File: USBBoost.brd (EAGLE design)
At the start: 43.8 x 20.3 mm, 27 parts, among them IC1 RT9276, J1 Input, J2 3.75V, J3 2.33V, J4 1.17V, J5 Status, X1 USB_

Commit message: foo
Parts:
- removed R15: 20k0, freetronics-original:0603
- added R3: 49k9, freetronics-original:0603
- R10: value 1k -> 130k
- R11: value 130k -> 73k2
- R12: value 73k2 -> 26k7
- R13: value 26k7 -> 20k
- R14: value 20k -> 20k0
- R5: value 49k9 -> 180k
- R6: value 180k -> 10k
- R8: value 10k -> 1k
- moved R8 17.0 mm to (15.9, 17.8), turned to 90 degrees
- moved R7 15.8 mm to (27.1, 5.08), turned to 0 degrees
- moved R14 9.38 mm to (18.4, 8.49), turned to 180 degrees
- moved R5 8.10 mm to (18.4, 6.83), turned to 180 degrees
- moved R6 7.21 mm to (12.4, 10.8), turned to 270 degrees
- moved R13 6.98 mm to (10.8, 14.0), turned to 270 degrees
- moved R10 6.35 mm to (8.89, 14.0)
- moved R12 2.86 mm to (3.81, 14.0)
- moved R4 2.77 mm to (26.0, 9.53), turned to 270 degrees
- moved R11 2.22 mm to (6.67, 14.0), turned to 180 degrees
- moved R9 1.90 mm to (14.0, 17.8)
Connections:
- net !LBO: now also R7.2; no longer R8.2
- net !PGOOD: now also R6.2; no longer R7.2
- net FB: now also R14.2, R5.2; no longer R15.2, R6.2
- net GND: now also R13.1, R3.2; no longer R15.1, R5.2
- net LBI: now also R10.1, R13.2; no longer R13.1, R14.2
- net N$10: now also R4.1; no longer R5.1
- net N$11: now also R11.2; no longer R12.2
- net N$12: now also R12.2; no longer R13.2
- net N$15: now also R9.2; no longer R10.2
- net N$5: now also R10.2; no longer R11.2
- net N$7: now also R3.1; no longer R4.1
- net N$8: now also R8.2; no longer R9.2
- net VOUT: now also R5.1; no longer R10.1
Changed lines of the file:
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@@
 <elements>
 <element name="C1" library="freetronics-jon" package="C0805" value="10uF" x="6.35" y="11.1125" smashed="yes"/>
-<element name="R15" library="freetronics-original" package="0603" value="20k0" x="18.415" y="8.493125" smashed="yes" rot="R180"/>
-<element name="R6" library="freetronics-original" package="0603" value="180k" x="18.399225" y="6.82625" smashed="yes" rot="R180"/>
+<element name="R14" library="freetronics-original" package="0603" value="20k0" x="18.415" y="8.493125" smashed="yes" rot="R180"/>
+<element name="R5" library="freetronics-original" package="0603" value="180k" x="18.399225" y="6.82625" smashed="yes" rot="R180"/>
 <element name="C2" library="freetronics-jon" package="C1206K" value="22uF" x="18.0975" y="3.4924" smashed="yes" rot="R90"/>
-<element name="R9" library="freetronics-original" package="0603" value="1k" x="15.875" y="17.78" smashed="yes" rot="R90"/>
+<element name="R8" library="freetronics-original" package="0603" value="1k" x="15.875" y="17.78" smashed="yes" rot="R90"/>
 <element name="J1" library="freetronics-master-v1" package="1X02" value="Input" x="1.90495" y="11.43" smashed="yes" rot="R270"/>
 <element name="X1" library="freetronics-master-v1" package="USB-A-S-SILK-FEMALE" value="USB_" x="36.83" y="10.16" smashed="yes" rot="R180"/>
 <element name="R2" library="freetronics-original" package="0603" value="75k" x="26.035" y="12.7" smashed="yes" rot="R270"/>
-<element name="R5" library="freetronics-original" package="0603" value="49k9" x="26.035" y="9.525" smashed="yes" rot="R270"/>
+<element name="R4" library="freetronics-original" package="0603" value="49k9" x="26.035" y="9.525" smashed="yes" rot="R270"/>
 <element name="R1" library="freetronics-original" package="0603" value="75k" x="22.621875" y="11.27125" smashed="yes" rot="R270"/>
-<element name="R4" library="freetronics-original" package="0603" value="49k9" x="23.33625" y="8.89" smashed="yes"/>
+<element name="R3" library="freetronics-original" package="0603" value="49k9" x="23.33625" y="8.89" smashed="yes"/>
 <element name="LED1" library="freetronics-master-v1" package="LED-0603" value="Power" x="17.78" y="17.78" smashed="yes" rot="R270"/>
 <element name="L1" library="freetronics-luke" package="CDRH" value="6.8 uH" x="7.62" y="5.715" smashed="yes" rot="R180"/>
@@
 <element name="J3" library="freetronics-luke" package="SJ" value="2.33V" x="6.35" y="17.145" smashed="yes" rot="R90"/>
 <element name="J4" library="freetronics-luke" package="SJ" value="1.17V" x="3.81" y="17.145" smashed="yes" rot="R90"/>
-<element name="R13" library="freetronics-original" package="0603" value="26k7" x="3.81" y="13.97" smashed="yes" rot="R180"/>
-<element name="R12" library="freetronics-original" package="0603" value="73k2" x="6.6675" y="13.97" smashed="yes" rot="R180"/>
-<element name="R11" library="freetronics-original" package="0603" value="130k" x="8.89" y="13.97" smashed="yes" rot="R90"/>
-<element name="R14" library="freetronics-original" package="0603" value="20k" x="10.795" y="13.97" smashed="yes" rot="R270"/>
-<element name="R7" library="freetronics-original" package="0603" value="10k" x="12.3825" y="10.795" smashed="yes" rot="R270"/>
-<element name="R8" library="freetronics-original" package="0603" value="10k" x="27.14625" y="5.08" smashed="yes"/>
-<element name="R10" library="freetronics-original" package="0603" value="1k" x="13.97" y="17.78" smashed="yes" rot="R90"/>
+<element name="R12" library="freetronics-original" package="0603" value="26k7" x="3.81" y="13.97" smashed="yes" rot="R180"/>
+<element name="R11" library="freetronics-original" package="0603" value="73k2" x="6.6675" y="13.97" smashed="yes" rot="R180"/>
+<element name="R10" library="freetronics-original" package="0603" value="130k" x="8.89" y="13.97" smashed="yes" rot="R90"/>
+<element name="R13" library="freetronics-original" package="0603" value="20k" x="10.795" y="13.97" smashed="yes" rot="R270"/>
+<element name="R6" library="freetronics-original" package="0603" value="10k" x="12.3825" y="10.795" smashed="yes" rot="R270"/>
+<element name="R7" library="freetronics-original" package="0603" value="10k" x="27.14625" y="5.08" smashed="yes"/>
+<element name="R9" library="freetronics-original" package="0603" value="1k" x="13.97" y="17.78" smashed="yes" rot="R90"/>
 <element name="LED2" library="freetronics-master-v1" package="LED-0603" value="Low Batt" x="12.065" y="17.78" smashed="yes" rot="R270"/>
 <element name="J5" library="freetronics-master-v1" package="1X02" value="Status" x="28.575" y="2.54" smashed="yes" rot="R180"/>
@@
 <signal name="GND">
 <contactref element="C1" pad="2"/>
-<contactref element="R15" pad="1"/>
+<contactref element="R14" pad="1"/>
 <contactref element="C2" pad="2"/>
-<contactref element="R5" pad="2"/>
 <contactref element="R4" pad="2"/>
+<contactref element="R3" pad="2"/>
 <contactref element="LED1" pad="C"/>
 <polygon width="0.4064" layer="1" isolate="0.4064">
@@
 <vertex x="-0.635" y="0"/>
 </polygon>
-<contactref element="R14" pad="1"/>
+<contactref element="R13" pad="1"/>
 <contactref element="J1" pad="2"/>
 <contactref element="X1" pad="GND"/>
@@
 <via x="10.795" y="15.875" extent="1-16" drill="0.5"/>
 <via x="15.875" y="14.605" extent="1-16" drill="0.5"/>
-<wire x1="14.97" y1="4.24" x2="15.67" y2="4.24" width="0.3048" layer="1"/>
+<wire x1="14.97" y1="4.24" x2="15.67" y2="4.24" width="0.2794" layer="1"/>
 <wire x1="15.67" y1="4.24" x2="15.875" y2="4.445" width="0.3048" layer="1"/>
 <wire x1="15.875" y1="4.445" x2="15.875" y2="5.23875" width="0.3048" layer="1"/>
@@
 </signal>
 <signal name="FB">
-<contactref element="R6" pad="2"/>
-<contactref element="R15" pad="2"/>
+<contactref element="R5" pad="2"/>
+<contactref element="R14" pad="2"/>
 <contactref element="IC1" pad="3"/>
 <wire x1="13.97" y1="4.24" x2="13.97" y2="2.619375" width="0.254" layer="1"/>
@@
 </signal>
 <signal name="N$8">
-<contactref element="R9" pad="2"/>
+<contactref element="R8" pad="2"/>
 <contactref element="LED1" pad="A"/>
 <wire x1="15.875" y1="18.542" x2="17.78" y2="18.542" width="0.4064" layer="1"/>
@@
 </signal>
 <signal name="VOUT">
-<contactref element="R6" pad="1"/>
-<contactref element="R9" pad="1"/>
+<contactref element="R5" pad="1"/>
+<contactref element="R8" pad="1"/>
 <contactref element="C2" pad="1"/>
 <contactref element="R2" pad="1"/>
 <contactref element="R1" pad="1"/>
 <contactref element="F1" pad="1"/>
+<contactref element="R6" pad="1"/>
 <contactref element="R7" pad="1"/>
-<contactref element="R8" pad="1"/>
-<contactref element="R10" pad="1"/>
+<contactref element="R9" pad="1"/>
 <contactref element="IC1" pad="2"/>
 <wire x1="13.47" y1="4.24" x2="13.47" y2="3.46875" width="0.254" layer="1"/>
@@
 <signal name="N$7">
 <contactref element="R1" pad="2"/>
-<contactref element="R4" pad="1"/>
+<contactref element="R3" pad="1"/>
 <contactref element="X1" pad="D-"/>
 <via x="27.305" y="8.255" extent="1-16" drill="0.5"/>
@@
 <signal name="N$10">
 <contactref element="R2" pad="2"/>
-<contactref element="R5" pad="1"/>
+<contactref element="R4" pad="1"/>
 <contactref element="X1" pad="D+"/>
 <wire x1="29.618" y1="11.16" x2="26.813" y2="11.16" width="0.6096" layer="1"/>
@@
 <signal name="N$5">
 <contactref element="J2" pad="1"/>
-<contactref element="R11" pad="2"/>
+<contactref element="R10" pad="2"/>
 <wire x1="8.89" y1="14.732" x2="8.89" y2="16.383" width="0.6096" layer="1"/>
 </signal>
 <signal name="N$11">
 <contactref element="J3" pad="1"/>
-<contactref element="R12" pad="2"/>
+<contactref element="R11" pad="2"/>
 <wire x1="5.9055" y1="13.97" x2="5.9055" y2="14.1605" width="0.6096" layer="1"/>
 <wire x1="5.9055" y1="14.1605" x2="6.35" y2="14.605" width="0.6096" layer="1"/>
@@
 <signal name="N$12">
 <contactref element="J4" pad="1"/>
-<contactref element="R13" pad="2"/>
+<contactref element="R12" pad="2"/>
 <wire x1="3.048" y1="13.97" x2="3.048" y2="14.081125" width="0.6096" layer="1"/>
 <wire x1="3.048" y1="14.081125" x2="3.81" y2="14.843125" width="0.6096" layer="1"/>
@@
 </signal>
 <signal name="!PGOOD">
-<contactref element="R7" pad="2"/>
+<contactref element="R6" pad="2"/>
 <contactref element="J5" pad="1"/>
 <contactref element="IC1" pad="8"/>
@@
 </signal>
 <signal name="!LBO">
-<contactref element="R8" pad="2"/>
+<contactref element="R7" pad="2"/>
 <contactref element="LED2" pad="C"/>
 <contactref element="J5" pad="2"/>
@@
 </signal>
 <signal name="N$15">
-<contactref element="R10" pad="2"/>
+<contactref element="R9" pad="2"/>
 <contactref element="LED2" pad="A"/>
 <wire x1="12.065" y1="18.542" x2="13.97" y2="18.542" width="0.4064" layer="1"/>
 </signal>
 <signal name="LBI">
+<contactref element="R10" pad="1"/>
+<contactref element="R12" pad="1"/>
+<contactref element="R13" pad="2"/>
 <contactref element="R11" pad="1"/>
-<contactref element="R13" pad="1"/>
-<contactref element="R14" pad="2"/>
-<contactref element="R12" pad="1"/>
 <wire x1="8.937625" y1="13.160375" x2="8.89" y2="13.208" width="0.4064" layer="1"/>
 <contactref element="IC1" pad="7"/>

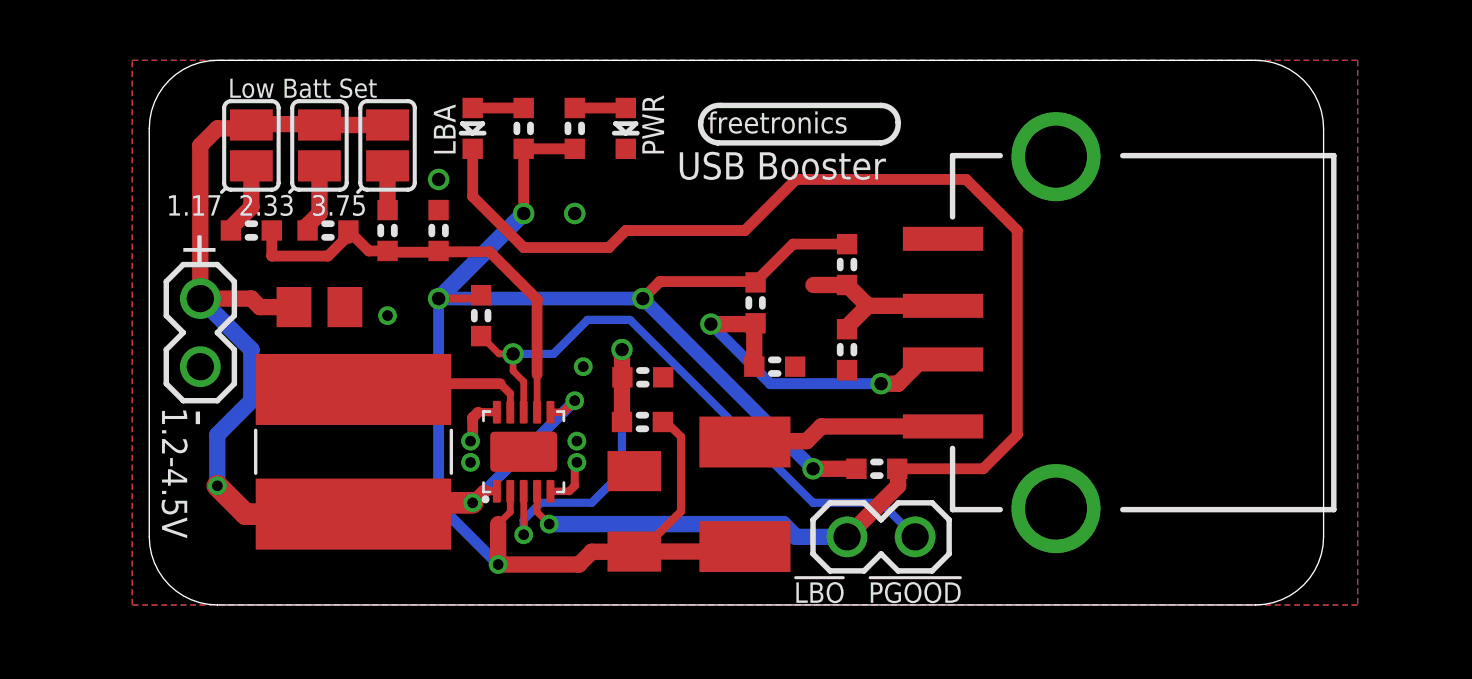
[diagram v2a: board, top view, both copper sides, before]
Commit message: Layout and schematic tweaks
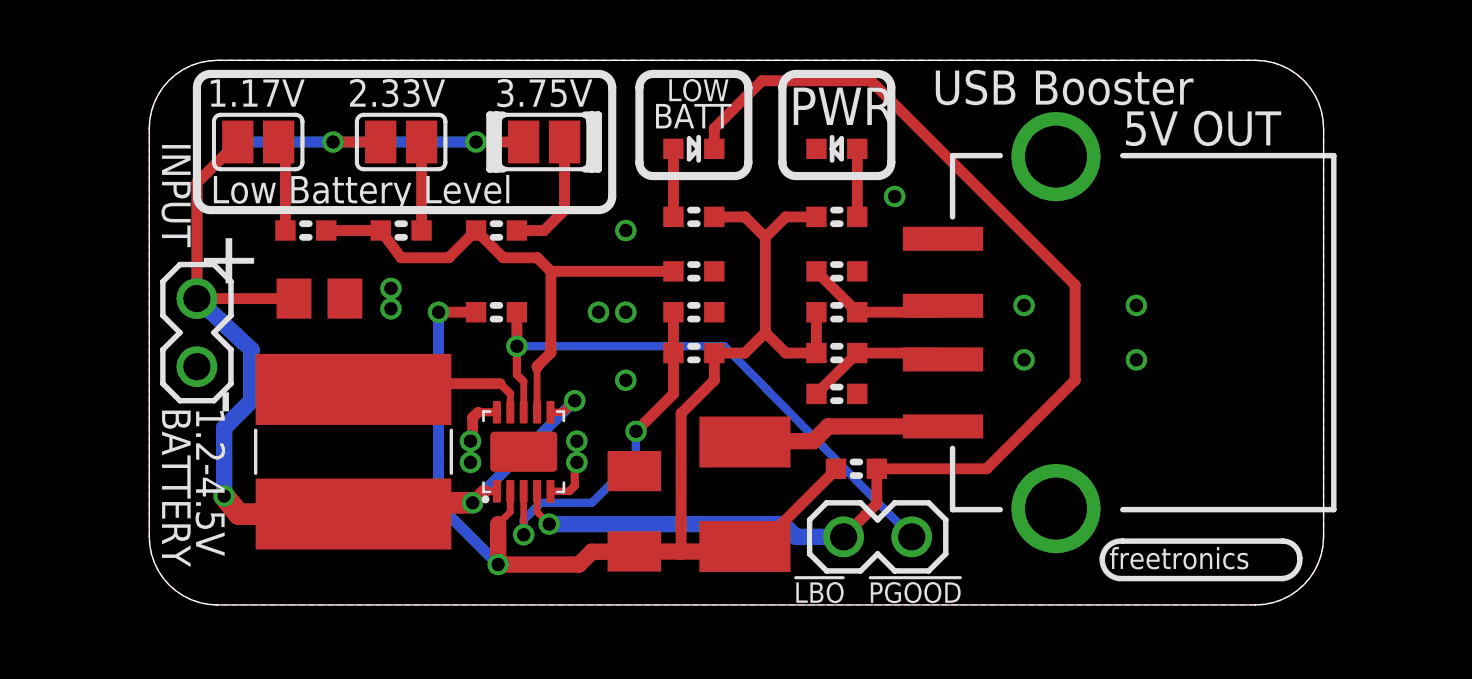
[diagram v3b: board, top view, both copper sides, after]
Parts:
- moved R8 10.3 mm to (25.7, 14.5), turned to 0 degrees
- moved R13 9.65 mm to (20.3, 12.4), turned to 180 degrees
- moved LED2 8.29 mm to (20.3, 17.0), turned to 0 degrees
- moved LED1 7.91 mm to (25.7, 17.0), turned to 180 degrees
- moved R9 7.16 mm to (20.3, 14.5), turned to 180 degrees
- moved J2 5.84 mm to (14.7, 17.3), turned to 180 degrees
- moved R10 4.06 mm to (13.0, 14.0), turned to 0 degrees
- moved R1 3.56 mm to (25.7, 9.40), turned to 0 degrees
- moved R5 3.21 mm to (20.3, 9.40)
- moved R14 3.09 mm to (20.3, 10.9)
- moved J3 3.05 mm to (9.40, 17.3), turned to 180 degrees
- moved R4 2.95 mm to (25.7, 12.4), turned to 0 degrees
- moved R11 2.73 mm to (9.40, 14.0), turned to 0 degrees
- moved R3 2.53 mm to (25.7, 7.87)
- moved R12 2.03 mm to (5.84, 14.0)
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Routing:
- net VOUT: track 66.6 -> 52.3 mm, vias 5 -> 2
- net VBAT: track 43.3 -> 55.3 mm, vias 3 -> 5
- net N$7: track 13.5 -> 5.61 mm, vias 2 -> 0
- net !LBO: track 53.4 -> 46.1 mm
- net LBI: track 16.8 -> 20.0 mm
- net N$5: track 1.65 -> 4.63 mm
- net !PGOOD: track 22.7 -> 21.6 mm
- net FB: track 14.5 -> 13.3 mm
- net N$10: track 6.35 -> 5.46 mm
- net N$11: track 2.60 -> 3.30 mm
- net N$12: track 2.73 -> 3.41 mm
- net N$8: track 1.91 -> 2.54 mm
- net N$15: track 1.91 -> 2.54 mm
- net GND: vias 8 -> 15
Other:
- board text added: "(C)2012 Freetronics Pty Ltd"
- board text added: "1.17V"
- board text added: "2.33V"
- board text added: "3.75V"
- board text added: "5V OUT"
- board text added: "BATT"
- board text added: "BATTERY"
- board text added: "INPUT"
- board text added: "LOW"
- board text added: "Low Battery Level"
- board text added: "v1.0"
- board text removed: "1.17"
- board text removed: "2.33"
- board text removed: "3.75"
- board text removed: "LBA"
- board text removed: "Low Batt Set"
